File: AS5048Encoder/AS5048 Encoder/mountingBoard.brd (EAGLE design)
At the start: 50 x 30 mm, 0 parts

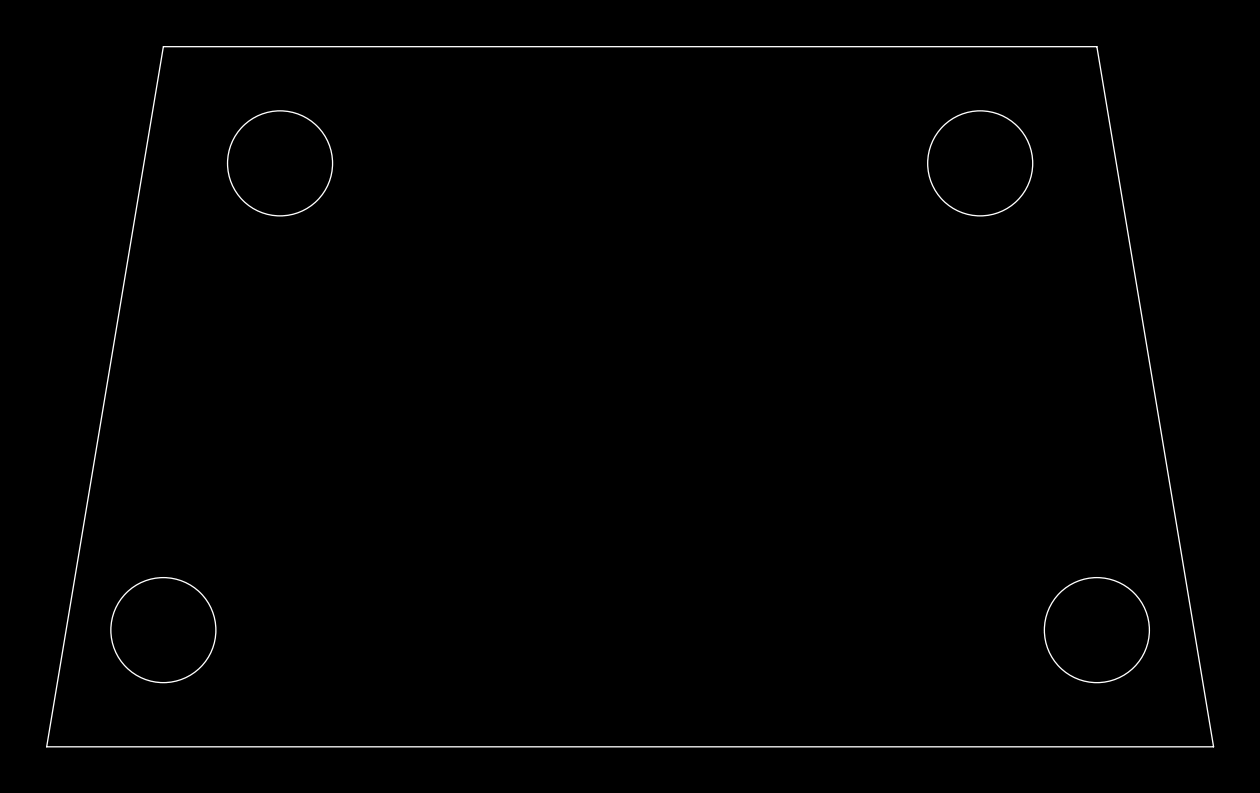
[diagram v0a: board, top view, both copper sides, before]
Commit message: rounded corners
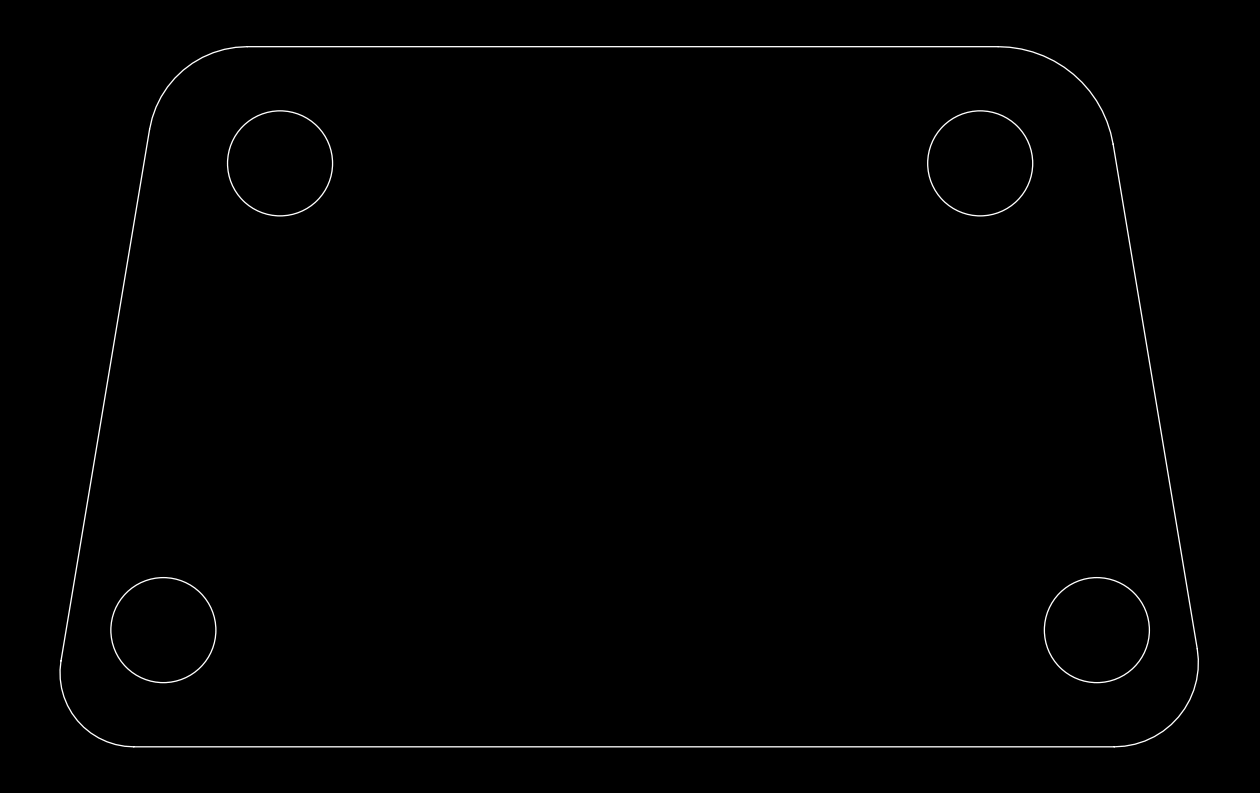
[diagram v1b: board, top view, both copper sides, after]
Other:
- board size 50 x 30 mm -> 48.8 x 30 mm
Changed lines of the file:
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@@
 <board>
 <plain>
-<wire x1="0" y1="0" x2="5" y2="30" width="0" layer="20"/>
-<wire x1="5" y1="30" x2="45" y2="30" width="0" layer="20"/>
-<wire x1="50" y1="0" x2="45" y2="30" width="0" layer="20"/>
+<wire x1="45.743790625" y1="0" x2="3.732940625" y2="0" width="0" layer="20"/>
+<wire x1="3.732940625" y1="0" x2="0.613690625" y2="3.68214375" width="0" layer="20" curve="-99.462211"/>
+<wire x1="0.613690625" y1="3.68214375" x2="4.409140625" y2="26.45484375" width="0" layer="20"/>
+<wire x1="4.409140625" y1="26.45484375" x2="8.59405625" y2="30" width="0" layer="20" curve="-80.537657"/>
+<wire x1="45.696334375" y1="25.82199375" x2="49.300284375" y2="4.19829375" width="0" layer="20"/>
+<wire x1="49.300284375" y1="4.19829375" x2="45.743790625" y2="0" width="0" layer="20" curve="-99.462339"/>
+<wire x1="45.696334375" y1="25.82199375" x2="40.764365625" y2="30" width="0" layer="20" curve="80.53769"/>
+<wire x1="40.764365625" y1="30" x2="8.59405625" y2="30" width="0" layer="20"/>
 <hole x="5" y="5" drill="4.5"/>
 <hole x="45" y="5" drill="4.5"/>
-<wire x1="50" y1="0" x2="0" y2="0" width="0" layer="20"/>
 <hole x="10" y="25" drill="4.5"/>
 <hole x="40" y="25" drill="4.5"/>
